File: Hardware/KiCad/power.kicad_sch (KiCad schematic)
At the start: 54 parts, among them U6 TP6841S6, U7 TPS73233

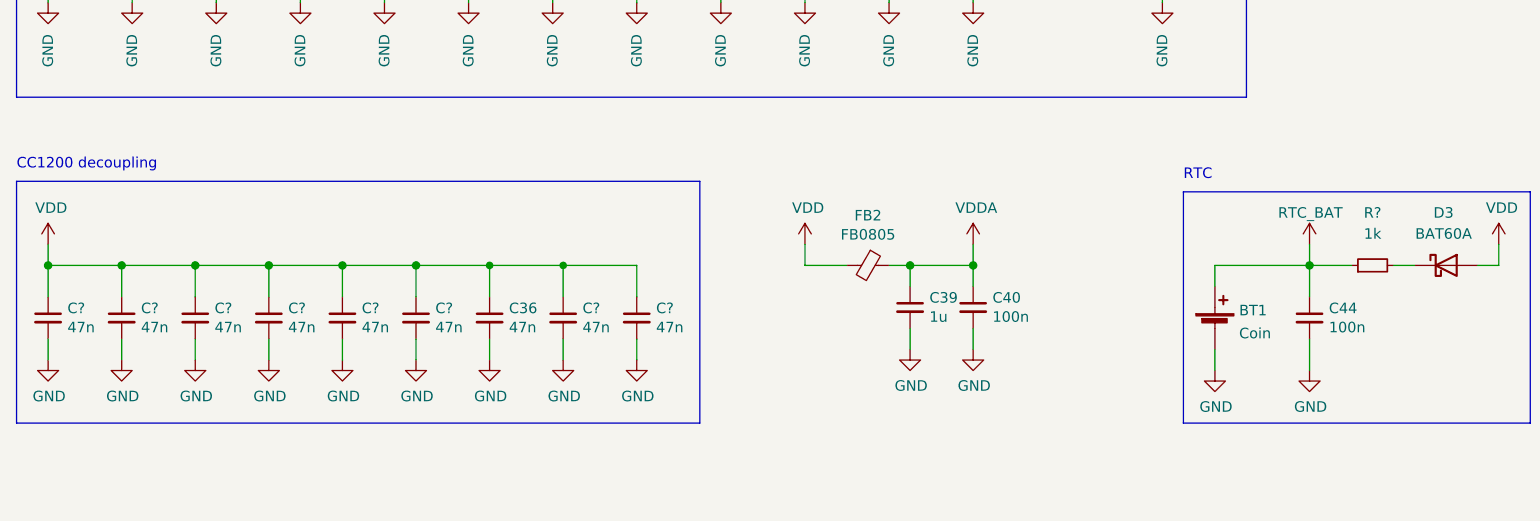
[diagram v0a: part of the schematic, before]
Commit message: Add no connection labels, anotate schematic, regen pdf and create netlist
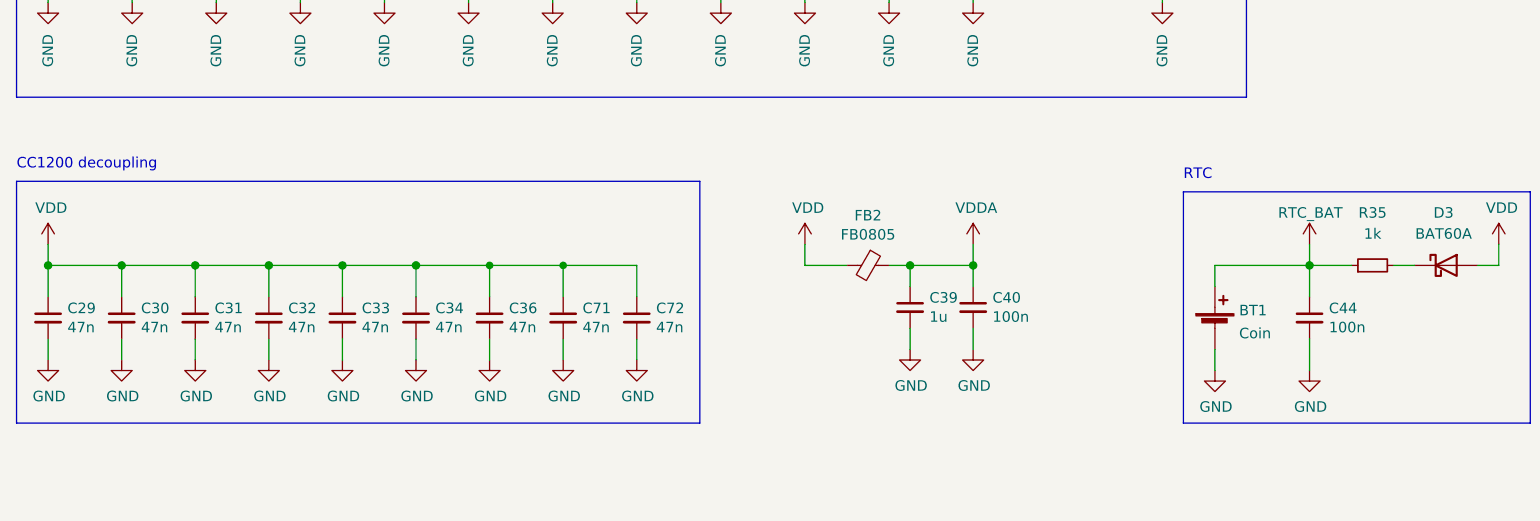
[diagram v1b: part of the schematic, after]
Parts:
- gave numbers to parts that had none: 9
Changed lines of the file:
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@@
   (symbol (lib_id "pkl_device:pkl_C_Small") (at 41.91 147.32 0) (unit 1)
     (in_bom yes) (on_board yes)
-    (property "Reference" "C?" (id 0) (at 44.2468 146.1516 0)
+    (property "Reference" "C30" (id 0) (at 44.2468 146.1516 0)
       (effects (font (size 1.27 1.27)) (justify left))
     )
@@
   (symbol (lib_id "pkl_device:pkl_C_Small") (at 50.8 147.32 0) (unit 1)
     (in_bom yes) (on_board yes)
-    (property "Reference" "C?" (id 0) (at 53.1368 146.1516 0)
+    (property "Reference" "C31" (id 0) (at 53.1368 146.1516 0)
       (effects (font (size 1.27 1.27)) (justify left))
     )
@@
   (symbol (lib_id "pkl_device:pkl_C_Small") (at 68.58 147.32 0) (unit 1)
     (in_bom yes) (on_board yes)
-    (property "Reference" "C?" (id 0) (at 70.9168 146.1516 0)
+    (property "Reference" "C33" (id 0) (at 70.9168 146.1516 0)
       (effects (font (size 1.27 1.27)) (justify left))
     )
@@
   (symbol (lib_id "power:GND") (at 104.14 152.4 0) (unit 1)
     (in_bom yes) (on_board yes)
-    (property "Reference" "#PWR?" (id 0) (at 104.14 158.75 0)
+    (property "Reference" "#PWR0208" (id 0) (at 104.14 158.75 0)
       (effects (font (size 1.27 1.27)) hide)
     )
@@
   (symbol (lib_id "pkl_device:pkl_C_Small") (at 77.47 147.32 0) (unit 1)
     (in_bom yes) (on_board yes)
-    (property "Reference" "C?" (id 0) (at 79.8068 146.1516 0)
+    (property "Reference" "C34" (id 0) (at 79.8068 146.1516 0)
       (effects (font (size 1.27 1.27)) (justify left))
     )
@@
   (symbol (lib_id "pkl_device:pkl_R_Small") (at 193.04 140.97 90) (unit 1)
     (in_bom yes) (on_board yes) (fields_autoplaced)
-    (property "Reference" "R?" (id 0) (at 193.04 134.62 90))
+    (property "Reference" "R35" (id 0) (at 193.04 134.62 90))
     (property "Value" "1k" (id 1) (at 193.04 137.16 90))
     (property "Footprint" "Resistor_SMD:R_0402_1005Metric" (id 2) (at 193.04 140.97 0)
@@
   (symbol (lib_id "power:VDD") (at 33.02 95.25 0) (unit 1)
     (in_bom yes) (on_board yes)
-    (property "Reference" "#PWR?" (id 0) (at 33.02 99.06 0)
+    (property "Reference" "#PWR0222" (id 0) (at 33.02 99.06 0)
       (effects (font (size 1.27 1.27)) hide)
     )
@@
   (symbol (lib_id "power:GND") (at 95.25 152.4 0) (unit 1)
     (in_bom yes) (on_board yes)
-    (property "Reference" "#PWR?" (id 0) (at 95.25 158.75 0)
+    (property "Reference" "#PWR0221" (id 0) (at 95.25 158.75 0)
       (effects (font (size 1.27 1.27)) hide)
     )
@@
   (symbol (lib_id "power:VDD") (at 208.28 138.43 0) (unit 1)
     (in_bom yes) (on_board yes)
-    (property "Reference" "#PWR?" (id 0) (at 208.28 142.24 0)
+    (property "Reference" "#PWR0186" (id 0) (at 208.28 142.24 0)
       (effects (font (size 1.27 1.27)) hide)
     )
@@
   (symbol (lib_id "pkl_device:pkl_C_Small") (at 59.69 147.32 0) (unit 1)
     (in_bom yes) (on_board yes)
-    (property "Reference" "C?" (id 0) (at 62.0268 146.1516 0)
+    (property "Reference" "C32" (id 0) (at 62.0268 146.1516 0)
       (effects (font (size 1.27 1.27)) (justify left))
     )
@@
   (symbol (lib_id "pkl_device:pkl_C_Small") (at 104.14 147.32 0) (unit 1)
     (in_bom yes) (on_board yes)
-    (property "Reference" "C?" (id 0) (at 106.4768 146.1516 0)
+    (property "Reference" "C72" (id 0) (at 106.4768 146.1516 0)
       (effects (font (size 1.27 1.27)) (justify left))
     )
@@
   (symbol (lib_id "pkl_device:pkl_C_Small") (at 95.25 147.32 0) (unit 1)
     (in_bom yes) (on_board yes)
-    (property "Reference" "C?" (id 0) (at 97.5868 146.1516 0)
+    (property "Reference" "C71" (id 0) (at 97.5868 146.1516 0)
       (effects (font (size 1.27 1.27)) (justify left))
     )
@@
   (symbol (lib_id "pkl_device:pkl_C_Small") (at 33.02 147.32 0) (unit 1)
     (in_bom yes) (on_board yes)
-    (property "Reference" "C?" (id 0) (at 35.3568 146.1516 0)
-      (effects (font (size 1.27 1.27)) (justify left))
-    )
+    (property "Reference" "C29" (id 0) (at 35.3568 146.1516 0)
+      (effects (font (size 1.27 1.27)) (justify left))
+    )
